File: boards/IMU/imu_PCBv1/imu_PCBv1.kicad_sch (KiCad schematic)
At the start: 30 parts, among them J1 USB_B_Mini, J2 SWD_Header, J4 Micro_SD_Card_Det1, J5 UART, J6 CAN_Bus, U1 ISM330DLCTR, U2 STM32F103RBT6, U3 SN65HVD230, U4 AP2112K-3.3, Y1 8MHz

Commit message: Organized first draft of schematic
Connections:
- net 3.3V: now also C2.2; no longer C2.1
- net GND: now also C2.1; no longer C2.2
- net SWDIO: now reaches J2.1 (SWDIO), U2.46 (PA13)
- net SWCLK: now reaches J2.2 (SWCLK), U2.49 (PA14)
- net NRST: now reaches C9.2, J2.5 (NRST), U2.7 (~{RST})
- net DET: now reaches J4.9 (DET), U2.8 (PC0)
- net USART2_TX: now reaches J5.2 (USART2_TX), U2.16 (PA2)
- net USART2_RX: now reaches J5.3 (USART2_RX), U2.17 (PA3)
- net R: now reaches U2.44 (PA11), U3.4 (R)
- net D: now reaches U2.45 (PA12), U3.1 (D)
- net INT1: now reaches U1.4 (INT1), U2.58 (PB6)
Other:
- note added: "CAN Transceiver"
- note added: "IMU Sensor"
- note added: "Mini-B USB Connector 3.3V Converter"
- note added: "SWD Header Pins"
- note added: "UART Debugger"
- note added: "microSD Card"
- moved on the sheet: C1, C10, C11, C12, C13, C14, C2, C3, C4, C5, C6, C7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

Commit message: Changed USB-B Mini to USB-C
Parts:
- removed J1: USB_B_Mini, symbol Connector:USB_B_Mini
- added P1: USB_C_Plug_USB2.0, Package_DFN_QFN:WDFN-10-1EP_3x3mm_P0.5mm_EP1.8x2.5mm, symbol Connector:USB_C_Plug_USB2.0
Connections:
- net GND: now also P1.A1 (GND), P1.A12 (GND), P1.B1 (GND), P1.B12 (GND)
- net at C11.2, U4.1 (VIN), U4.3 (EN): now also P1.A4 (VBUS), P1.A9 (VBUS), P1.B4 (VBUS), P1.B9 (VBUS)
- no-connect marks 44 -> 45
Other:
- moved on the sheet: C11, C12, U4

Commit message: Added 5.1k resistor to CC pin of USB-C
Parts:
- added R7: 5.1k, symbol Device:R
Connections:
- net GND: now also R7.2
- net at P1.A5 (CC): now also R7.1
- no-connect marks 45 -> 44
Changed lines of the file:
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@@
 	)
 	(no_connect
-		(at 252.73 120.65)
-	)
-	(no_connect
 		(at 170.18 55.88)
 	)
@@
 	(wire
 		(pts
+			(xy 246.38 128.27) (xy 246.38 132.08)
+		)
+		(stroke
+			(width 0)
+			(type default)
+		)
+	)
+	(wire
+		(pts
 			(xy 223.52 142.24) (xy 227.33 142.24)
 		)
@@
 	(wire
 		(pts
+			(xy 246.38 120.65) (xy 252.73 120.65)
+		)
+		(stroke
+			(width 0)
+			(type default)
+		)
+	)
+	(wire
+		(pts
 			(xy 160.02 146.05) (xy 160.02 148.59)
 		)
@@
 	(symbol
 		(lib_id "Device:R")
+		(at 246.38 124.46 0)
+		(unit 1)
+		(body_style 1)
+		(exclude_from_sim no)
+		(in_bom yes)
+		(on_board yes)
+		(in_pos_files yes)
+		(dnp no)
+		(fields_autoplaced yes)
+		(property "Reference" "R7"
+			(at 248.92 123.1899 0)
+			(show_name no)
+			(do_not_autoplace no)
+			(effects
+				(font
+					(size 1.27 1.27)
+				)
+				(justify left)
+			)
+		)
+		(property "Value" "5.1k"
+			(at 248.92 125.7299 0)
+			(show_name no)
+			(do_not_autoplace no)
+			(effects
+				(font
+					(size 1.27 1.27)
+				)
+				(justify left)
+			)
+		)
+		(property "Footprint" ""
+			(at 244.602 124.46 90)
+			(hide yes)
+			(show_name no)
+			(do_not_autoplace no)
+			(effects
+				(font
+					(size 1.27 1.27)
+				)
+			)
+		)
+		(property "Datasheet" ""
+			(at 246.38 124.46 0)
+			(hide yes)
+			(show_name no)
+			(do_not_autoplace no)
+			(effects
+				(font
+					(size 1.27 1.27)
+				)
+			)
+		)
+		(property "Description" "Resistor"
+			(at 246.38 124.46 0)
+			(hide yes)
+			(show_name no)
+			(do_not_autoplace no)
+			(effects
+				(font
+					(size 1.27 1.27)
+				)
+			)
+		)
+		(pin "1"
+		)
+		(pin "2"
+		)
+		(instances
+			(project "imu_PCBv1"
+				(path "/c751f12b-4428-40a4-afa3-9f787be38c4a"
+					(reference "R7")
+					(unit 1)
+				)
+			)
+		)
+	)
+	(symbol
+		(lib_id "Device:R")
 		(at 160.02 142.24 0)
 		(unit 1)
@@
 					(unit 1)
 				)
+			)
+		)
+	)
+	(symbol
+		(lib_id "power:GND")
+		(at 246.38 132.08 0)
+		(unit 1)
+		(body_style 1)
+		(exclude_from_sim no)
+		(in_bom yes)
+		(on_board yes)
+		(in_pos_files yes)
+		(dnp no)
+		(fields_autoplaced yes)
+		(property "Reference" "#PWR031"
+			(at 246.38 138.43 0)
+			(hide yes)
+			(show_name no)
+			(do_not_autoplace no)
+			(effects
+				(font
+					(size 1.27 1.27)
+				)
+			)
+		)
+		(property "Value" "GND"
+			(at 246.38 137.16 0)
+			(show_name no)
+			(do_not_autoplace no)
+			(effects
+				(font
+					(size 1.27 1.27)
+				)
+			)
+		)
+		(property "Footprint" ""
+			(at 246.38 132.08 0)
+			(hide yes)
+			(show_name no)
+			(do_not_autoplace no)
+			(effects
+				(font
+					(size 1.27 1.27)
+				)
+			)
+		)
+		(property "Datasheet" ""
+			(at 246.38 132.08 0)
+			(hide yes)
+			(show_name no)
+			(do_not_autoplace no)
+			(effects
+				(font
+					(size 1.27 1.27)
+				)
+			)
+		)
+		(property "Description" "Power symbol creates a global label with name \"GND\" , ground"
+			(at 246.38 132.08 0)
+			(hide yes)
+			(show_name no)
+			(do_not_autoplace no)
+			(effects
+				(font
+					(size 1.27 1.27)
+				)
+			)
+		)
+		(pin "1"
+		)
+		(instances
+			(project "imu_PCBv1"
+				(path "/c751f12b-4428-40a4-afa3-9f787be38c4a"
+					(reference "#PWR031")
+					(unit 1)
+				)

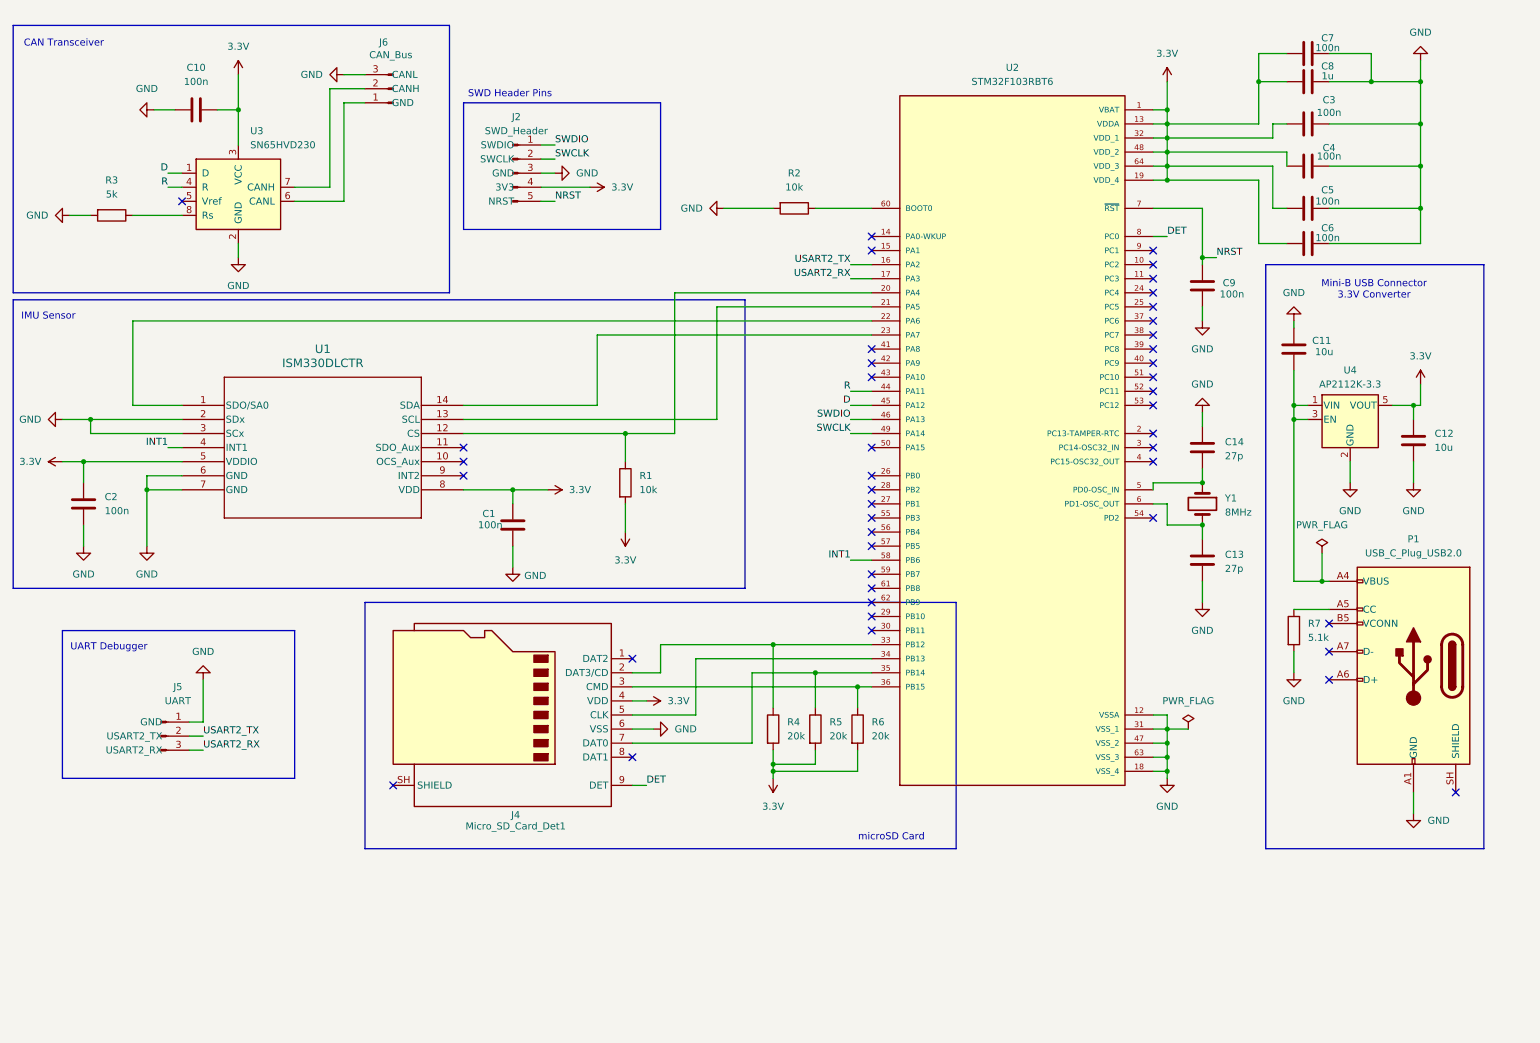
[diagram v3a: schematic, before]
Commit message: Fixed schematic, fixed footprints, started layout
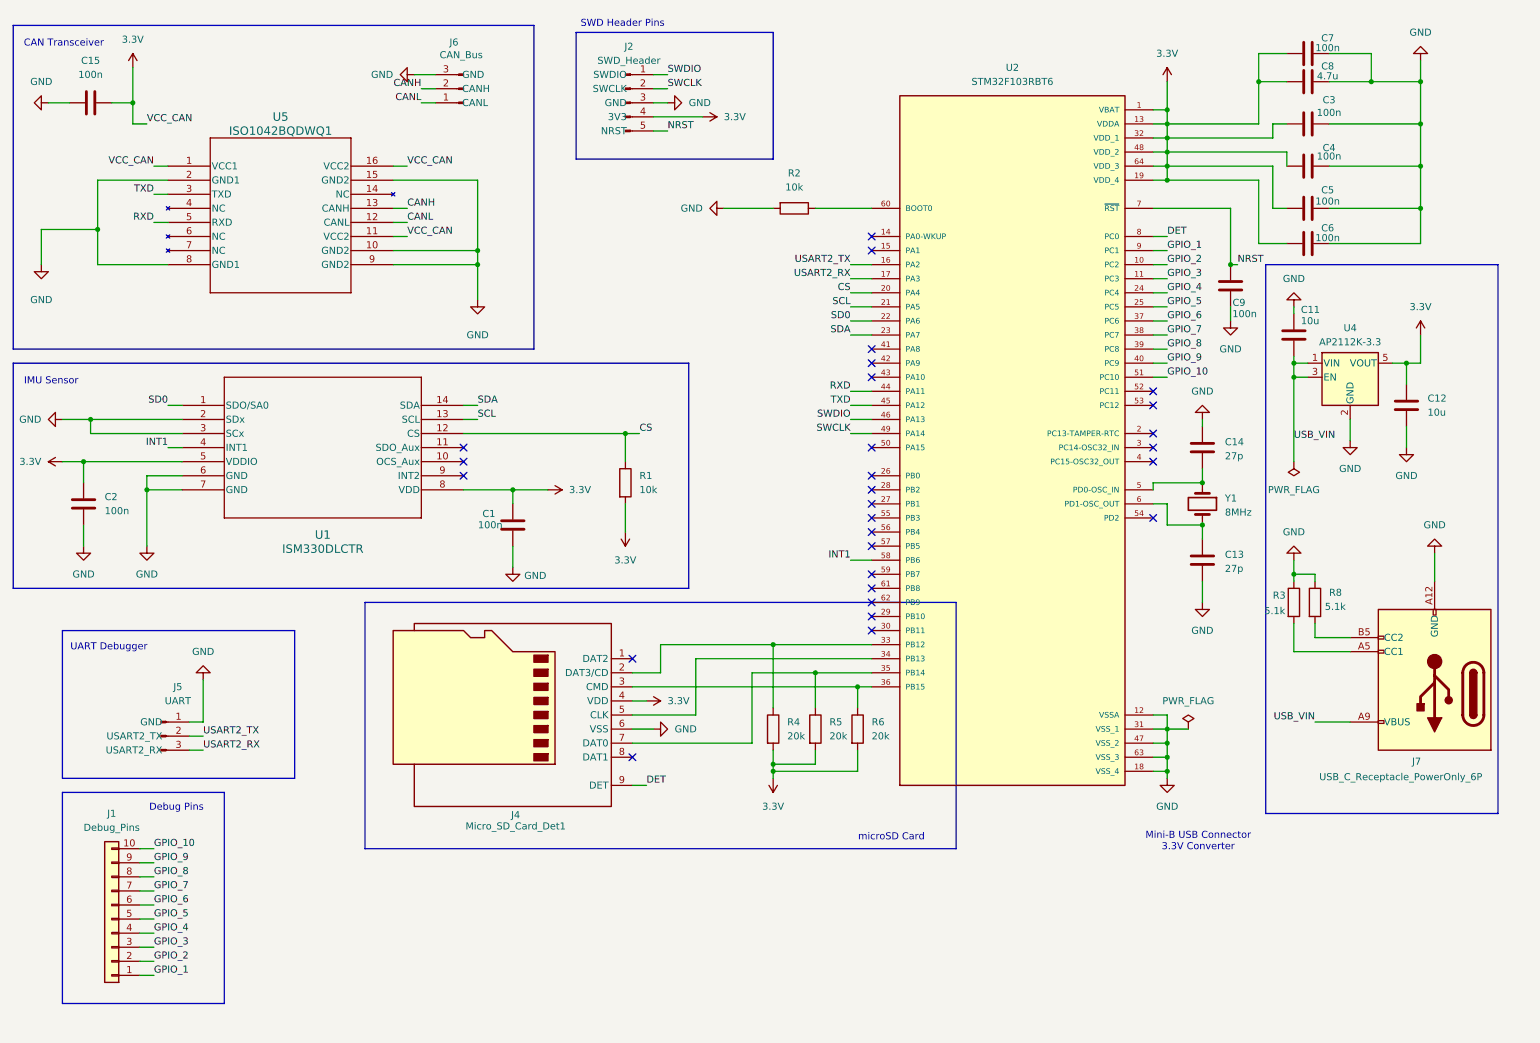
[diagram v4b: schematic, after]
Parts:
- removed C10: 100n, Package_SO:SOIC-8_3.9x4.9mm_P1.27mm, symbol Device:C
- removed P1: USB_C_Plug_USB2.0, Package_DFN_QFN:WDFN-10-1EP_3x3mm_P0.5mm_EP1.8x2.5mm, symbol Connector:USB_C_Plug_USB2.0
- removed R7: 5.1k, symbol Device:R
- removed U3: SN65HVD230, Package_SO:SOIC-8_3.9x4.9mm_P1.27mm, symbol Interface_CAN_LIN:SN65HVD230
- added C15: 100n, Capacitor_SMD:C_0603_1608Metric_Pad1.08x0.95mm_HandSolder, symbol Device:C
- added J1: Debug_Pins, Connector_PinHeader_2.54mm:PinHeader_1x10_P2.54mm_Vertical, symbol Connector_Generic:Conn_01x10
- added J7: USB_C_Receptacle_PowerOnly_6P, imu_footprints:USB_Connector, symbol Connector:USB_C_Receptacle_PowerOnly_6P
- added R8: 5.1k, Resistor_SMD:R_0603_1608Metric_Pad0.98x0.95mm_HandSolder, symbol Device:R
- added U5: ISO1042BQDWQ1, imu_footprints:CAN-M, symbol ISM330DLC:ISO1042BQDWQ1
- C1, C2, C3, C4, C5, C6, C7, C9: footprint (none) -> Capacitor_SMD:C_0603_1608Metric_Pad1.08x0.95mm_HandSolder
- C11, C12, C13, C14: footprint Package_SO:SOIC-8_3.9x4.9mm_P1.27mm -> Capacitor_SMD:C_0603_1608Metric_Pad1.08x0.95mm_HandSolder
- C8: value 1u -> 4.7u; footprint (none) -> Capacitor_SMD:C_0603_1608Metric_Pad1.08x0.95mm_HandSolder
- J2: footprint Package_SIP:Sanyo_STK4xx-15_59.2x8.0mm_P2.54mm -> Connector_PinHeader_2.54mm:PinHeader_1x05_P2.54mm_Vertical
- J4: footprint (none) -> imu_footprints:microSD_CardConnector_MSD-4-A
- J5, J6: footprint Package_SIP:Sanyo_STK4xx-15_59.2x8.0mm_P2.54mm -> Connector:FanPinHeader_1x03_P2.54mm_Vertical
- R1: footprint (none) -> Resistor_SMD:R_0603_1608Metric_Pad0.98x0.95mm_HandSolder
- R2, R4, R5, R6: footprint Package_DIP:DIP-8_W7.62mm -> Resistor_SMD:R_0603_1608Metric_Pad0.98x0.95mm_HandSolder
- R3: value 5k -> 5.1k; footprint Package_DIP:DIP-8_W7.62mm -> Resistor_SMD:R_0603_1608Metric_Pad0.98x0.95mm_HandSolder
- U1: footprint LGA-14L_2P5X3X0P83_STM -> imu_footprints:ISM330DLCTR-M
- U2: footprint STM32F103RBT6:QFP50P1200X1200X160-64N -> imu_footprints:STM32F103RBT6-10x10mm
- U4: footprint Package_TO_SOT_SMD:SOT-23-5 -> imu_footprints:LinearRegulator_DIO-M
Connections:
- net 3.3V: now also C15.2, U5.1 (VCC1), U5.11 (VCC2), U5.16 (VCC2)
- net GND: now also R3.1, C15.1, J7.A12 (GND), J7.B12 (GND), R8.1, U5.10 (GND2), U5.15 (GND2), U5.2 (GND1), U5.8 (GND1), U5.9 (GND2); no longer R3.2
- net USB_VIN: now reaches C11.2, U4.1 (VIN), U4.3 (EN)
- net USB_VIN: now also J7.A9 (VBUS), J7.B9 (VBUS)
- net CS: now reaches R1.1, U1.12 (CS), U2.20 (PA4)
- net GPIO_2: now reaches U2.10 (PC2)
- net GPIO_2: now also J1.2 (Pin_2)
- net GPIO_3: now reaches U2.11 (PC3)
- net GPIO_3: now also J1.3 (Pin_3)
- net SCL: now reaches U1.13 (SCL), U2.21 (PA5)
- net SD0: now reaches U1.1 (SDO/SA0), U2.22 (PA6)
- net SDA: now reaches U1.14 (SDA), U2.23 (PA7)
- net GPIO_4: now reaches U2.24 (PC4)
- net GPIO_4: now also J1.4 (Pin_4)
- net GPIO_5: now reaches U2.25 (PC5)
- net GPIO_5: now also J1.5 (Pin_5)
- net GPIO_6: now reaches U2.37 (PC6)
- net GPIO_6: now also J1.6 (Pin_6)
- net GPIO_7: now reaches U2.38 (PC7)
- net GPIO_7: now also J1.7 (Pin_7)
- net GPIO_8: now reaches U2.39 (PC8)
- net GPIO_8: now also J1.8 (Pin_8)
- net GPIO_9: now reaches U2.40 (PC9)
- net GPIO_9: now also J1.9 (Pin_9)
- net GPIO_10: now reaches U2.51 (PC10)
- net GPIO_10: now also J1.10 (Pin_10)
- net GPIO_1: now reaches U2.9 (PC1)
- net GPIO_1: now also J1.1 (Pin_1)
- net CANL: now reaches J6.1 (CANL)
- net CANL: now also U5.12 (CANL)
- net CANH: now reaches J6.2 (CANH)
- net CANH: now also U5.13 (CANH)
- net D renamed TXD
- net TXD: now also U5.3 (TXD)
- net R renamed RXD
- net RXD: now also U5.5 (RXD)
- new net: J7.A5 (CC1), R3.2
- new net: J7.B5 (CC2), R8.2
- no-connect marks 44 -> 28
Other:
- note added: "Debug Pins"
- moved on the sheet: C11, C12, C9, J2, J6, U4

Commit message: First draft of IMU layout
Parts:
- removed J1: Debug_Pins, Connector_PinHeader_2.54mm:PinHeader_1x10_P2.54mm_Vertical, symbol Connector_Generic:Conn_01x10
- added J3: Conn_01x08_Pin, Connector_PinHeader_2.54mm:PinHeader_1x08_P2.54mm_Vertical, symbol Connector:Conn_01x08_Pin
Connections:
- net GPIO_10 is gone; now on net GPIO_7: U2.51 (PC10)
- net GPIO_1: now also U2.57 (PB5), J3.1 (Pin_1); no longer U2.9 (PC1)
- net GPIO_2: now also U2.56 (PB4), J3.2 (Pin_2); no longer U2.10 (PC2)
- net GPIO_3: now also U2.55 (PB3), J3.3 (Pin_3); no longer U2.11 (PC3)
- net GPIO_4: now also U2.54 (PD2), J3.4 (Pin_4); no longer U2.24 (PC4)
- net GPIO_5: now also U2.53 (PC12), J3.5 (Pin_5); no longer U2.25 (PC5)
- net GPIO_6: now also U2.52 (PC11), J3.6 (Pin_6); no longer U2.37 (PC6)
- net GPIO_7: now also J3.7 (Pin_7); no longer U2.38 (PC7)
- net GPIO_8: now also U2.50 (PA15), J3.8 (Pin_8); no longer U2.39 (PC8)
- net GPIO_9: no longer names the net of U2.40 (PC9)
- no-connect marks 28 -> 30
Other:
- moved on the sheet: C13, C14, Y1
